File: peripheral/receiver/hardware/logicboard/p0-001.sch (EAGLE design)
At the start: 23 parts, among them IC1 74LS07N, IC2 LTC485N, IC3 LTC485N

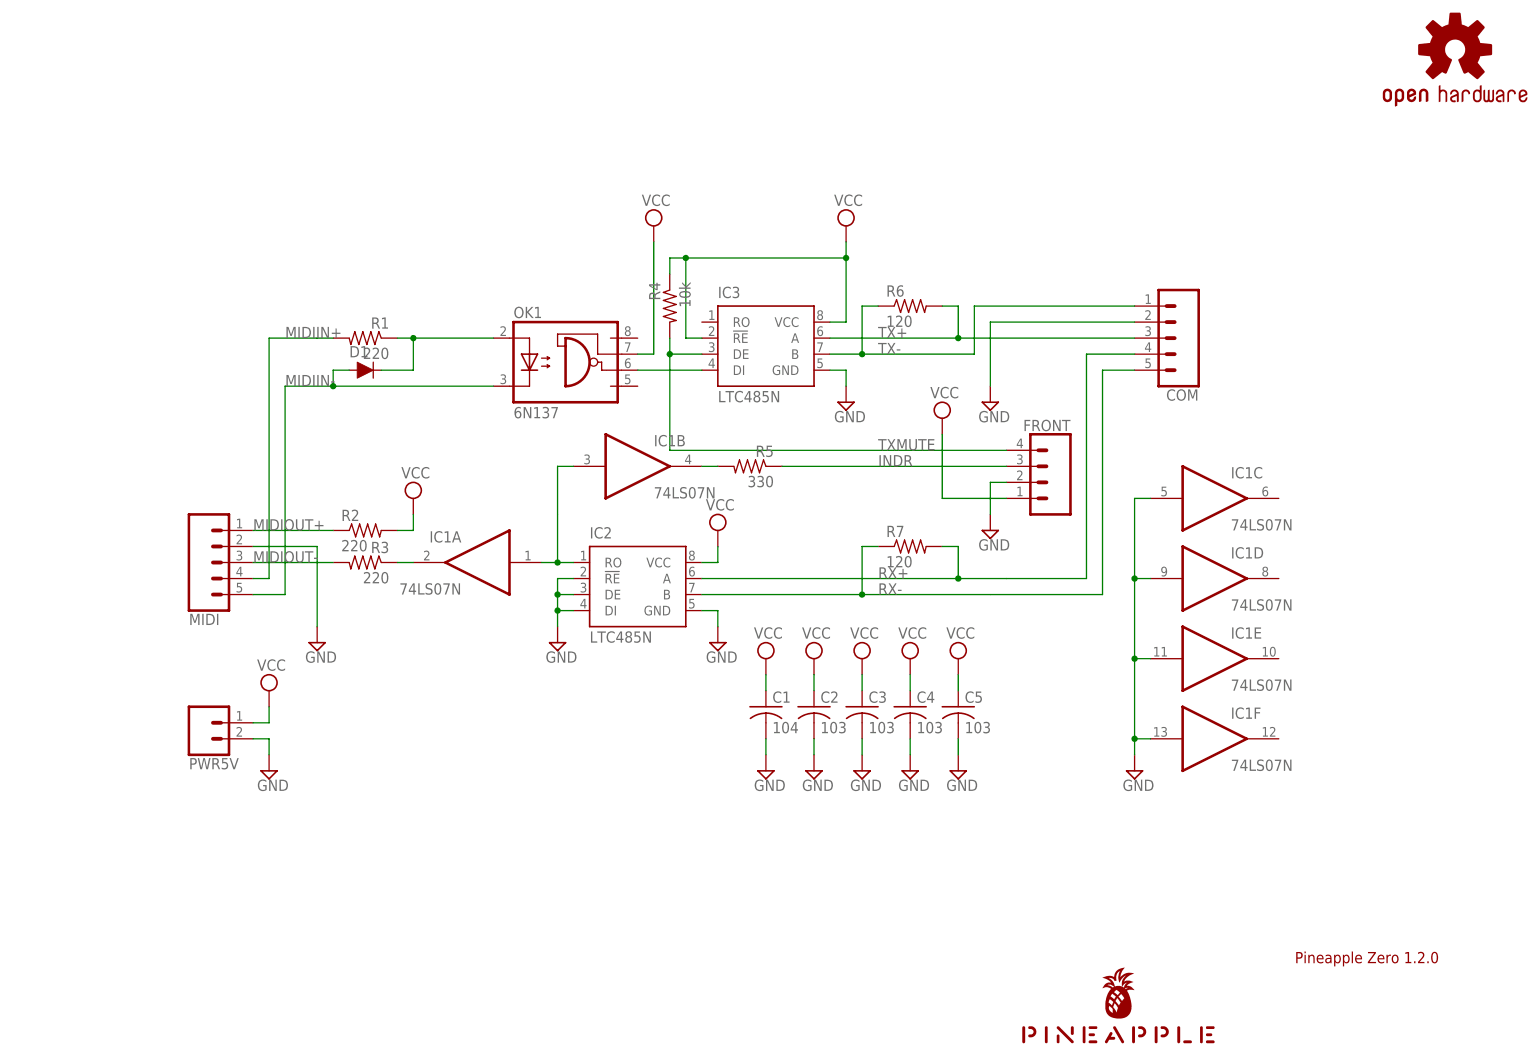
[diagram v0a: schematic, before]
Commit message: Added DX receiver.
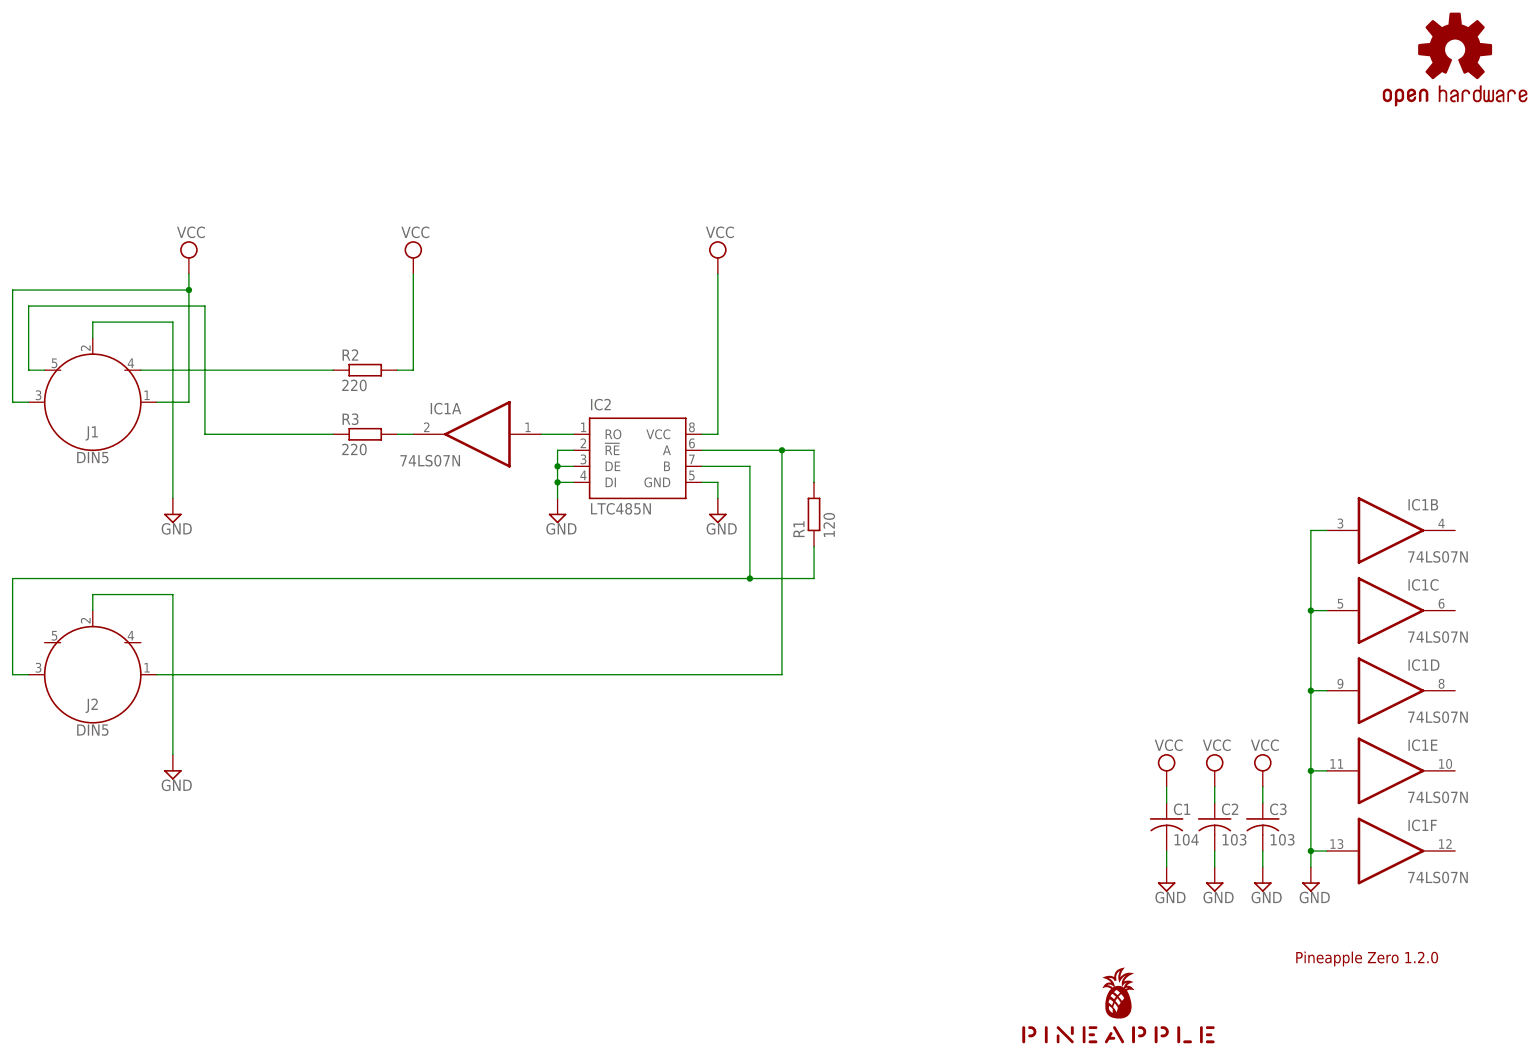
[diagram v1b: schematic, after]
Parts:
- removed C4, C5: 103, rcl:C-US025-025X050
- removed COM, MIDI: (no value), SparkFun-Connectors:CONN_05JST
- removed D1: DIODE-1N4148, SparkFun-DiscreteSemi:DIODE-1N4148
- removed FRONT: (no value), SparkFun-Connectors:CONN_04JST-PTH
- removed IC3: LTC485N, linear-technology:LTC485N
- removed OK1: 6N137, optocoupler:6N137
- removed PWR5V: (no value), SparkFun-Connectors:CONN_02JST-PTH-2
- removed R4: 10k, resistor:R-US_0204/5
- removed R5: 330, resistor:R-US_0204/5
- removed R6, R7: 120, resistor:R-US_0204/5
- added J1, J2: DIN5, SparkFun-Connectors:DIN5
- R1: value 220 -> 120; device resistor:R-US_0204/5 -> resistor:R-EU_0204/5
- R2, R3: device resistor:R-US_0204/5 -> resistor:R-EU_0204/5
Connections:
- removed net IND: IC1B.O, R5.2
- removed net INDR: FRONT.3, R5.1
- removed net MIDIIN: IC3.DI, OK1.VO
- removed net MIDIIN+: MIDI.4, R1.2
- removed net MIDIIN-: D1.A, MIDI.5, OK1.C
- removed net MIDIINA: D1.C, OK1.A, R1.1
- removed net MIDIOUT: IC1A.I, IC1B.I, IC2.RO
- removed net MIDIOUT+: MIDI.1, R2.1
- removed net MIDIOUT-: MIDI.3, R3.2
- removed net MIDIOUT-RAW: IC1A.O, R3.1
- removed net TX+: COM.3, IC3.A, R6.2
- removed net TX-: COM.1, IC3.B, R6.1
- removed net TXMUTE: FRONT.4, IC3.DE, R4.2
- new net MOUTRTN: J1.5, R3.1
- new net MOUTSND: J1.4, R2.1
- new net N$1: IC1A.O, R3.2
- new net TX: IC1A.I, IC2.RO
- net GND: now also IC1B.I, J1.2, J2.2; no longer C4.2, C5.2, COM.2, FRONT.2, IC3.GND, MIDI.2, PWR5V.2
- net RX+: now also J2.1, R1.2; no longer COM.4, R7.2
- net RX-: now also J2.3, R1.1; no longer COM.5, R7.1
- net VCC: now also J1.1, J1.3; no longer C4.1, C5.1, FRONT.1, IC3.!RE, IC3.VCC, OK1.VE, PWR5V.1, R4.1
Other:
- moved on the sheet: C1, C2, C3, IC1A, IC1B, IC1C, IC1D, IC1E, IC1F, IC2

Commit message: Alternative Qi connectors.
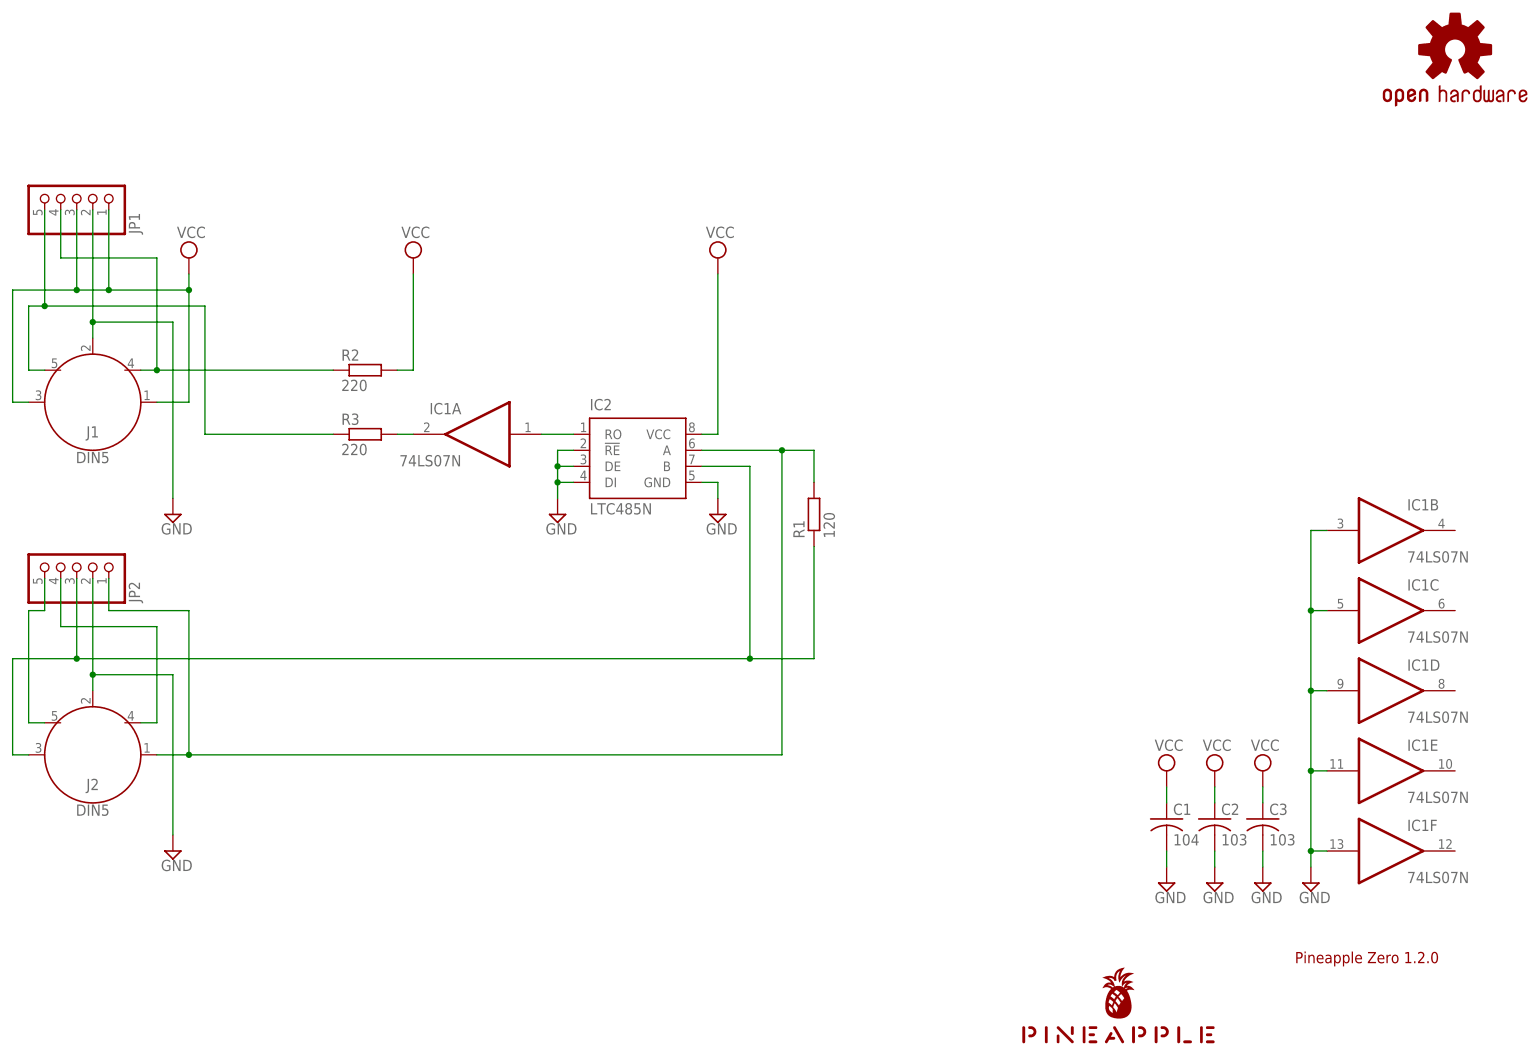
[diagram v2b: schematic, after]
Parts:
- added JP1, JP2: (no value), pinhead:PINHD-1X5
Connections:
- new net DUMMY4: J2.4, JP2.4
- new net DUMMY5: J2.5, JP2.5
- net GND: now also JP1.2, JP2.2
- net MOUTRTN: now also JP1.5
- net MOUTSND: now also JP1.4
- net RX+: now also JP2.1
- net RX-: now also JP2.3
- net VCC: now also JP1.1, JP1.3
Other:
- moved on the sheet: J2
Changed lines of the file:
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@@
 <setting verticaltext="up"/>
 </settings>
-<grid distance="0.1" unitdist="inch" unit="inch" style="dots" multiple="1" display="yes" altdistance="0.01" altunitdist="inch" altunit="inch"/>
+<grid distance="0.1" unitdist="inch" unit="inch" style="lines" multiple="1" display="no" altdistance="0.01" altunitdist="inch" altunit="inch"/>
 <layers>
 <layer number="1" name="Top" color="4" fill="1" visible="no" active="no"/>
@@
 <part name="R3" library="resistor" library_urn="urn:adsk.eagle:library:348" deviceset="R-EU_" device="0204/5" package3d_urn="urn:adsk.eagle:package:23488/1" value="220"/>
 <part name="SUPPLY2" library="supply2" library_urn="urn:adsk.eagle:library:372" deviceset="GND" device=""/>
+<part name="JP1" library="pinhead" library_urn="urn:adsk.eagle:library:325" deviceset="PINHD-1X5" device="" package3d_urn="urn:adsk.eagle:package:22469/2"/>
+<part name="JP2" library="pinhead" library_urn="urn:adsk.eagle:library:325" deviceset="PINHD-1X5" device="" package3d_urn="urn:adsk.eagle:package:22469/2"/>
 </parts>
 <sheets>
@@
 <attribute name="VALUE" x="25.4" y="101.346" size="1.778" layer="96" font="vector" align="top-center"/>
 </instance>
-<instance part="J2" gate="G$1" x="25.4" y="66.04" smashed="yes">
-<attribute name="NAME" x="25.4" y="60.452" size="1.778" layer="95" font="vector" align="bottom-center"/>
-<attribute name="VALUE" x="25.4" y="58.166" size="1.778" layer="96" font="vector" align="top-center"/>
+<instance part="J2" gate="G$1" x="25.4" y="53.34" smashed="yes">
+<attribute name="NAME" x="25.4" y="47.752" size="1.778" layer="95" font="vector" align="bottom-center"/>
+<attribute name="VALUE" x="25.4" y="45.466" size="1.778" layer="96" font="vector" align="top-center"/>
 </instance>
 <instance part="SUPPLY1" gate="GND" x="38.1" y="91.44" smashed="yes">
@@
 <attribute name="VALUE" x="64.77" y="100.838" size="1.778" layer="96"/>
 </instance>
-<instance part="SUPPLY2" gate="GND" x="38.1" y="50.8" smashed="yes">
-<attribute name="VALUE" x="36.195" y="47.625" size="1.778" layer="96"/>
+<instance part="SUPPLY2" gate="GND" x="38.1" y="38.1" smashed="yes">
+<attribute name="VALUE" x="36.195" y="34.925" size="1.778" layer="96"/>
+</instance>
+<instance part="JP1" gate="A" x="22.86" y="142.24" smashed="yes" rot="MR90">
+<attribute name="NAME" x="31.115" y="135.89" size="1.778" layer="95" rot="MR90"/>
+<attribute name="VALUE" x="12.7" y="135.89" size="1.778" layer="96" rot="MR90"/>
+</instance>
+<instance part="JP2" gate="A" x="22.86" y="83.82" smashed="yes" rot="MR90">
+<attribute name="NAME" x="31.115" y="77.47" size="1.778" layer="95" rot="MR90"/>
+<attribute name="VALUE" x="12.7" y="77.47" size="1.778" layer="96" rot="MR90"/>
 </instance>
 </instances>
@@
 <wire x1="25.4" y1="121.92" x2="38.1" y2="121.92" width="0.1524" layer="91"/>
 <wire x1="38.1" y1="121.92" x2="38.1" y2="93.98" width="0.1524" layer="91"/>
+<wire x1="25.4" y1="139.7" x2="25.4" y2="121.92" width="0.1524" layer="91"/>
+<junction x="25.4" y="121.92"/>
+<pinref part="JP1" gate="A" pin="2"/>
 </segment>
 <segment>
 <pinref part="J2" gate="G$1" pin="2"/>
-<wire x1="25.4" y1="76.2" x2="25.4" y2="78.74" width="0.1524" layer="91"/>
+<wire x1="25.4" y1="63.5" x2="25.4" y2="66.04" width="0.1524" layer="91"/>
 <pinref part="SUPPLY2" gate="GND" pin="GND"/>
-<wire x1="25.4" y1="78.74" x2="38.1" y2="78.74" width="0.1524" layer="91"/>
-<wire x1="38.1" y1="78.74" x2="38.1" y2="53.34" width="0.1524" layer="91"/>
+<wire x1="25.4" y1="66.04" x2="38.1" y2="66.04" width="0.1524" layer="91"/>
+<wire x1="38.1" y1="66.04" x2="38.1" y2="40.64" width="0.1524" layer="91"/>
+<wire x1="25.4" y1="81.28" x2="25.4" y2="66.04" width="0.1524" layer="91"/>
+<junction x="25.4" y="66.04"/>
+<pinref part="JP2" gate="A" pin="2"/>
 </segment>
 </net>
@@
 <wire x1="40.64" y1="127" x2="40.64" y2="109.22" width="0.1524" layer="91"/>
 <wire x1="40.64" y1="109.22" x2="35.56" y2="109.22" width="0.1524" layer="91"/>
-<wire x1="40.64" y1="127" x2="12.7" y2="127" width="0.1524" layer="91"/>
+<wire x1="40.64" y1="127" x2="27.94" y2="127" width="0.1524" layer="91"/>
 <junction x="40.64" y="127"/>
+<wire x1="27.94" y1="127" x2="22.86" y2="127" width="0.1524" layer="91"/>
+<wire x1="22.86" y1="127" x2="12.7" y2="127" width="0.1524" layer="91"/>
 <wire x1="12.7" y1="127" x2="12.7" y2="109.22" width="0.1524" layer="91"/>
 <pinref part="J1" gate="G$1" pin="3"/>
 <wire x1="12.7" y1="109.22" x2="15.24" y2="109.22" width="0.1524" layer="91"/>
+<wire x1="27.94" y1="139.7" x2="27.94" y2="127" width="0.1524" layer="91"/>
+<junction x="27.94" y="127"/>
+<wire x1="22.86" y1="139.7" x2="22.86" y2="127" width="0.1524" layer="91"/>
+<junction x="22.86" y="127"/>
+<pinref part="JP1" gate="A" pin="1"/>
+<pinref part="JP1" gate="A" pin="3"/>
 </segment>
 <segment>
@@
 <wire x1="121.92" y1="101.6" x2="134.62" y2="101.6" width="0.1524" layer="91"/>
 <pinref part="J2" gate="G$1" pin="1"/>
-<wire x1="35.56" y1="66.04" x2="134.62" y2="66.04" width="0.1524" layer="91"/>
-<wire x1="134.62" y1="66.04" x2="134.62" y2="101.6" width="0.1524" layer="91"/>
+<wire x1="35.56" y1="53.34" x2="40.64" y2="53.34" width="0.1524" layer="91"/>
+<wire x1="40.64" y1="53.34" x2="134.62" y2="53.34" width="0.1524" layer="91"/>
+<wire x1="134.62" y1="53.34" x2="134.62" y2="101.6" width="0.1524" layer="91"/>
 <wire x1="134.62" y1="101.6" x2="139.7" y2="101.6" width="0.1524" layer="91"/>
 <junction x="134.62" y="101.6"/>
 <pinref part="R1" gate="G$1" pin="2"/>
 <wire x1="139.7" y1="101.6" x2="139.7" y2="96.52" width="0.1524" layer="91"/>
+<wire x1="27.94" y1="81.28" x2="27.94" y2="76.2" width="0.1524" layer="91"/>
+<wire x1="27.94" y1="76.2" x2="40.64" y2="76.2" width="0.1524" layer="91"/>
+<wire x1="40.64" y1="76.2" x2="40.64" y2="53.34" width="0.1524" layer="91"/>
+<junction x="40.64" y="53.34"/>
+<pinref part="JP2" gate="A" pin="1"/>
 </segment>
 </net>
@@
 <pinref part="IC2" gate="G$1" pin="B"/>
 <wire x1="129.54" y1="99.06" x2="121.92" y2="99.06" width="0.1524" layer="91"/>
-<wire x1="12.7" y1="81.28" x2="129.54" y2="81.28" width="0.1524" layer="91"/>
-<wire x1="129.54" y1="81.28" x2="129.54" y2="99.06" width="0.1524" layer="91"/>
+<wire x1="12.7" y1="68.58" x2="22.86" y2="68.58" width="0.1524" layer="91"/>
+<wire x1="22.86" y1="68.58" x2="129.54" y2="68.58" width="0.1524" layer="91"/>
+<wire x1="129.54" y1="68.58" x2="129.54" y2="99.06" width="0.1524" layer="91"/>
 <pinref part="R1" gate="G$1" pin="1"/>
-<wire x1="139.7" y1="86.36" x2="139.7" y2="81.28" width="0.1524" layer="91"/>
-<wire x1="139.7" y1="81.28" x2="129.54" y2="81.28" width="0.1524" layer="91"/>
-<junction x="129.54" y="81.28"/>
+<wire x1="139.7" y1="86.36" x2="139.7" y2="68.58" width="0.1524" layer="91"/>
+<wire x1="139.7" y1="68.58" x2="129.54" y2="68.58" width="0.1524" layer="91"/>
+<junction x="129.54" y="68.58"/>
 <pinref part="J2" gate="G$1" pin="3"/>
-<wire x1="15.24" y1="66.04" x2="12.7" y2="66.04" width="0.1524" layer="91"/>
-<wire x1="12.7" y1="66.04" x2="12.7" y2="81.28" width="0.1524" layer="91"/>
+<wire x1="15.24" y1="53.34" x2="12.7" y2="53.34" width="0.1524" layer="91"/>
+<wire x1="12.7" y1="53.34" x2="12.7" y2="68.58" width="0.1524" layer="91"/>
+<wire x1="22.86" y1="81.28" x2="22.86" y2="68.58" width="0.1524" layer="91"/>
+<junction x="22.86" y="68.58"/>
+<pinref part="JP2" gate="A" pin="3"/>
 </segment>
 </net>
@@
 <pinref part="R2" gate="G$1" pin="1"/>
 <pinref part="J1" gate="G$1" pin="4"/>
-<wire x1="63.5" y1="114.3" x2="33.02" y2="114.3" width="0.1524" layer="91"/>
+<wire x1="63.5" y1="114.3" x2="35.56" y2="114.3" width="0.1524" layer="91"/>
+<wire x1="35.56" y1="114.3" x2="33.02" y2="114.3" width="0.1524" layer="91"/>
+<wire x1="20.32" y1="139.7" x2="20.32" y2="132.08" width="0.1524" layer="91"/>
+<wire x1="20.32" y1="132.08" x2="35.56" y2="132.08" width="0.1524" layer="91"/>
+<wire x1="35.56" y1="132.08" x2="35.56" y2="114.3" width="0.1524" layer="91"/>
+<junction x="35.56" y="114.3"/>
+<pinref part="JP1" gate="A" pin="4"/>
 </segment>
 </net>
@@
 <wire x1="17.78" y1="114.3" x2="15.24" y2="114.3" width="0.1524" layer="91"/>
 <wire x1="15.24" y1="114.3" x2="15.24" y2="124.46" width="0.1524" layer="91"/>
-<wire x1="15.24" y1="124.46" x2="43.18" y2="124.46" width="0.1524" layer="91"/>
+<wire x1="15.24" y1="124.46" x2="17.78" y2="124.46" width="0.1524" layer="91"/>
+<wire x1="17.78" y1="124.46" x2="43.18" y2="124.46" width="0.1524" layer="91"/>
 <wire x1="43.18" y1="124.46" x2="43.18" y2="104.14" width="0.1524" layer="91"/>
 <pinref part="R3" gate="G$1" pin="1"/>
 <wire x1="43.18" y1="104.14" x2="63.5" y2="104.14" width="0.1524" layer="91"/>
-</segment>
-</net>
+<wire x1="17.78" y1="139.7" x2="17.78" y2="124.46" width="0.1524" layer="91"/>
+<junction x="17.78" y="124.46"/>
+<pinref part="JP1" gate="A" pin="5"/>
+</segment>
+</net>
+<net name="DUMMY4" class="0">
+<segment>
+<pinref part="J2" gate="G$1" pin="4"/>
+<wire x1="33.02" y1="58.42" x2="35.56" y2="58.42" width="0.1524" layer="91"/>
+<wire x1="35.56" y1="58.42" x2="35.56" y2="73.66" width="0.1524" layer="91"/>
+<wire x1="35.56" y1="73.66" x2="20.32" y2="73.66" width="0.1524" layer="91"/>
+<wire x1="20.32" y1="73.66" x2="20.32" y2="81.28" width="0.1524" layer="91"/>
+<pinref part="JP2" gate="A" pin="4"/>
+</segment>
+</net>
+<net name="DUMMY5" class="0">
+<segment>
+<pinref part="J2" gate="G$1" pin="5"/>
+<wire x1="17.78" y1="58.42" x2="15.24" y2="58.42" width="0.1524" layer="91"/>
+<wire x1="15.24" y1="58.42" x2="15.24" y2="76.2" width="0.1524" layer="91"/>
+<wire x1="15.24" y1="76.2" x2="17.78" y2="76.2" width="0.1524" layer="91"/>
+<wire x1="17.78" y1="76.2" x2="17.78" y2="81.28" width="0.1524" layer="91"/>
+<pinref part="JP2" gate="A" pin="5"/>
+</segment>
+</net>
